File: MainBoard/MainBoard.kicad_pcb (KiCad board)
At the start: 2 copper layers, 39.6 x 110 mm, 29 parts, among them U1 TL074CN, U2 TL074CN, U3 TL074CN

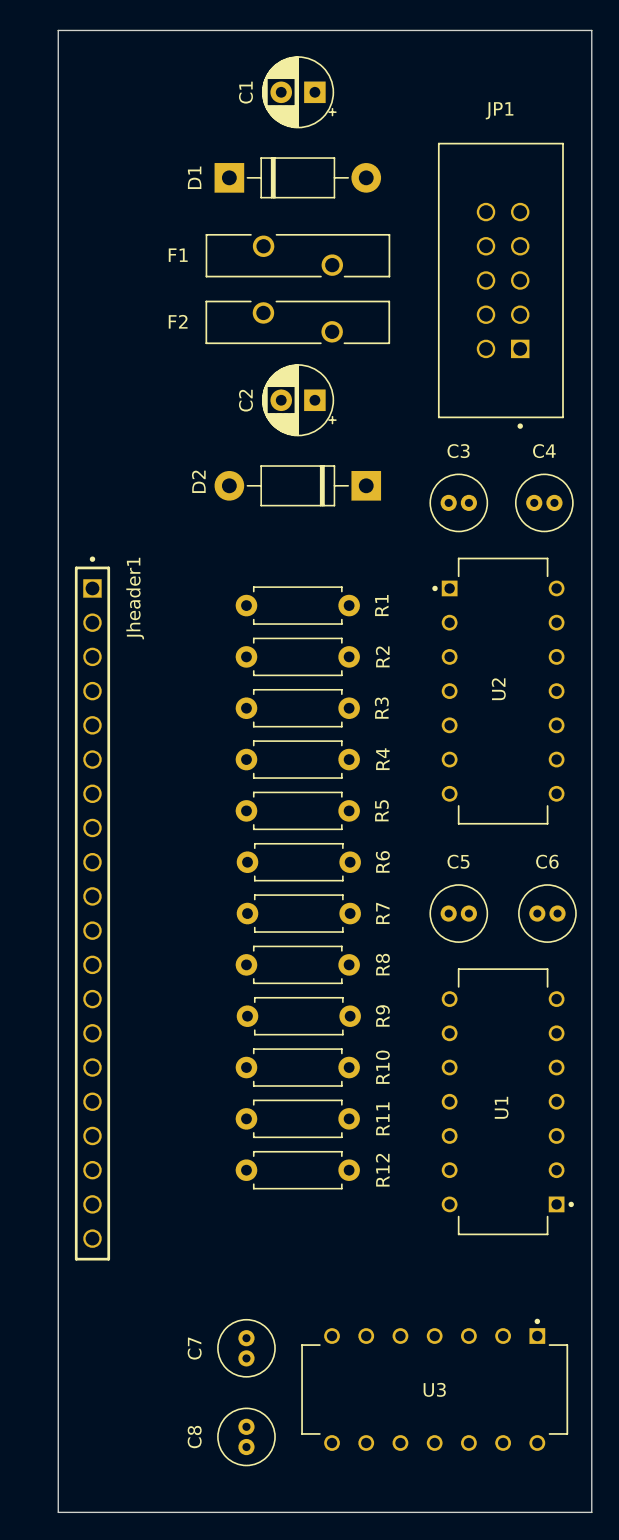
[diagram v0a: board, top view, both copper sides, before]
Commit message: updated with new footprints and 3d models
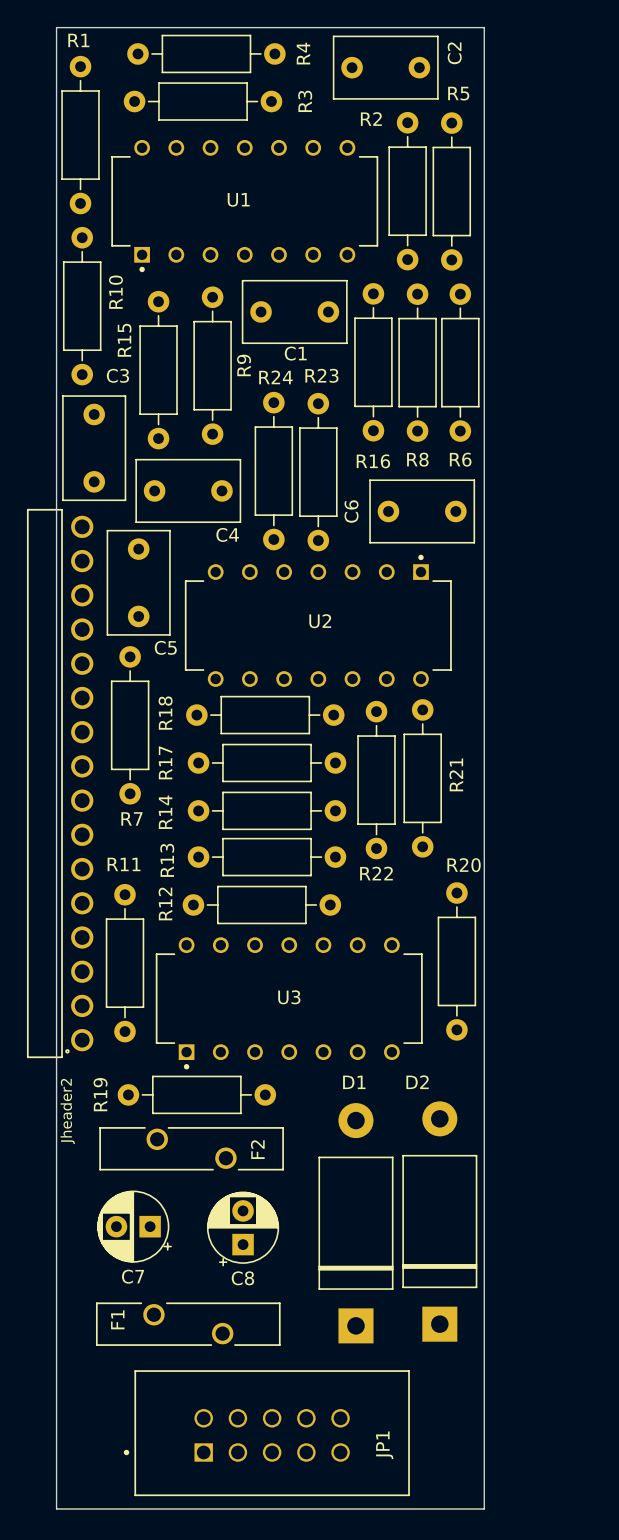
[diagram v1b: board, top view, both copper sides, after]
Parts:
- removed Jheader1: ESQ-120-12-T-S, ESQ-120-12-T-S:SAMTEC_ESQ-120-12-T-S
- added Jheader2: 61301611021, 61301611021:61301611021, F.Cu at (154.2, 98.3)
- added R13: 1k, Resistor_THT:R_Axial_DIN0207_L6.3mm_D2.5mm_P10.16mm_Horizontal, F.Cu at (162.8, 103.8)
- added R14: 1k, Resistor_THT:R_Axial_DIN0207_L6.3mm_D2.5mm_P10.16mm_Horizontal, F.Cu at (162.8, 100.3)
- added R15: 1M, Resistor_THT:R_Axial_DIN0207_L6.3mm_D2.5mm_P10.16mm_Horizontal, F.Cu at (159.8, 72.7)
- added R16: 100k, Resistor_THT:R_Axial_DIN0207_L6.3mm_D2.5mm_P10.16mm_Horizontal, F.Cu at (175.8, 62.0)
- added R17: 100k, Resistor_THT:R_Axial_DIN0207_L6.3mm_D2.5mm_P10.16mm_Horizontal, F.Cu at (173.0, 96.8)
- added R18: 100k, Resistor_THT:R_Axial_DIN0207_L6.3mm_D2.5mm_P10.16mm_Horizontal, F.Cu at (172.8, 93.2)
- added R19: 100k, Resistor_THT:R_Axial_DIN0207_L6.3mm_D2.5mm_P10.16mm_Horizontal, F.Cu at (167.8, 121.4)
- added R20: 100k, Resistor_THT:R_Axial_DIN0207_L6.3mm_D2.5mm_P10.16mm_Horizontal, F.Cu at (182.0, 116.6)
- added R21: 100k, Resistor_THT:R_Axial_DIN0207_L6.3mm_D2.5mm_P10.16mm_Horizontal, F.Cu at (179.5, 103.0)
- added R22: 100k, Resistor_THT:R_Axial_DIN0207_L6.3mm_D2.5mm_P10.16mm_Horizontal, F.Cu at (176.0, 93.0)
- added R23: 100k, Resistor_THT:R_Axial_DIN0207_L6.3mm_D2.5mm_P10.16mm_Horizontal, F.Cu at (171.7, 70.1)
- added R24: 100k, Resistor_THT:R_Axial_DIN0207_L6.3mm_D2.5mm_P10.16mm_Horizontal, F.Cu at (168.4, 70.0)
- C1, C2: value 10uf -> 0.1uf; footprint Capacitor_THT:CP_Radial_D5.0mm_P2.50mm -> Capacitor_THT:C_Disc_D7.5mm_W4.4mm_P5.00mm
- C3, C4, C5, C6: footprint Capacitor_THT:C_Radial_D4.0mm_H5.0mm_P1.50mm -> Capacitor_THT:C_Disc_D7.5mm_W4.4mm_P5.00mm
- C7, C8: value 0.1uf -> 10uf; footprint Capacitor_THT:C_Radial_D4.0mm_H5.0mm_P1.50mm -> Capacitor_THT:CP_Radial_D5.0mm_P2.50mm
- D1, D2: value 1N5818 -> 1N5934B; footprint Diode_THT:D_DO-41_SOD81_P10.16mm_Horizontal -> 1N5934B:P2_DO-201
- F1, F2: value Polyfuse -> type="R" model="Polyfuse" lib=""
- R1, R11, R12, R2, R3, R4, R5, R6, R7, R8: footprint Resistor_THT:R_Axial_DIN0207_L6.3mm_D2.5mm_P7.62mm_Horizontal -> Resistor_THT:R_Axial_DIN0207_L6.3mm_D2.5mm_P10.16mm_Horizontal
- R10, R9: value 1k -> 100k; footprint Resistor_THT:R_Axial_DIN0207_L6.3mm_D2.5mm_P7.62mm_Horizontal -> Resistor_THT:R_Axial_DIN0207_L6.3mm_D2.5mm_P10.16mm_Horizontal
- moved JP1 85.2 mm to (163.2, 148.0), turned to 0 degrees
- moved F1 79.7 mm to (162.1, 138.4)
- moved D1 78.2 mm to (174.5, 130.9), turned to 90 degrees
- moved U1 69.5 mm to (166.2, 55.1), turned to 90 degrees
- moved R10 62.8 mm to (154.2, 57.8), turned to -90 degrees
- moved F2 61.8 mm to (162.3, 125.4), turned to 180 degrees
- moved D2 54.9 mm to (180.7, 130.8), turned to 90 degrees
- moved R9 53.4 mm to (163.9, 62.2), turned to -90 degrees
- moved R5 53.3 mm to (181.6, 49.3), turned to -90 degrees
- moved R4 53.0 mm to (158.3, 44.1)
- moved R8 51.4 mm to (179.1, 62.0), turned to -90 degrees
- moved R3 45.8 mm to (158.1, 47.7)
- moved R6 45.0 mm to (182.2, 62.0), turned to -90 degrees
- moved R1 41.9 mm to (154.1, 45.1), turned to -90 degrees
- moved C5 36.5 mm to (158.4, 80.9), turned to -90 degrees
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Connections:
- C1 pad 2: -v -> GND
- C2 pad 2: Net-(C4-Pad1) -> GND
- C3 pad 2: -v -> GND
- C4 pad 1: Net-(C4-Pad1) -> -v
- C4 pad 2: -v -> GND
- C5 pad 2: -v -> GND
- C6 pad 1: Net-(C4-Pad1) -> -v
- C6 pad 2: -v -> GND
- C7 pad 2: -v -> GND
- C8 pad 1: Net-(C4-Pad1) -> GND
- D1 pad 2: -v -> GND
- D2 pad 1: -v -> GND
- D2 pad 2: Net-(C4-Pad1) -> -v
- F2 pad 1: Net-(C4-Pad1) -> -v
- JP1 pad 3: -v -> GND
- JP1 pad 4: -v -> GND
- JP1 pad 5: -v -> GND
- JP1 pad 6: -v -> GND
- JP1 pad 7: -v -> GND
- JP1 pad 8: -v -> GND
- R10 pad 1: Output6 -> Net-(U1-2IN+)
- R10 pad 2: Net-(R10-Pad2) -> InputBus1
- R11 pad 1: Output7 -> Output9
- R11 pad 2: Net-(R11-Pad2) -> Net-(U3-1IN-)
- R12 pad 1: Output8 -> Output12
- R5 pad 1: Output9 -> Output5
- R6 pad 1: Output10 -> Output6
- R7 pad 1: Output11 -> Output7
- R7 pad 2: Net-(R7-Pad2) -> Net-(U2-3IN-)
- R8 pad 1: Output12 -> Output8
- R8 pad 2: Net-(R7-Pad2) -> Net-(U2-4IN-)
- R9 pad 1: Output5 -> Net-(U1-1IN+)
- R9 pad 2: Net-(R9-Pad2) -> InputBus1
- U1 pad 10: InputBus1 -> Net-(U1-3IN+)
- U1 pad 3: InputBus1 -> Net-(U1-1IN+)
- U1 pad 5: InputBus1 -> Net-(U1-2IN+)
- U2 pad 10: InputBus4 -> Net-(U2-3IN+)
- U2 pad 12: InputBus4 -> Net-(U2-4IN+)
- U2 pad 13: Net-(R7-Pad2) -> Net-(U2-4IN-)
- U2 pad 14: Net-(R7-Pad2) -> Net-(U2-4IN-)
- U2 pad 3: InputBus3 -> Net-(U2-1IN+)
- U2 pad 5: InputBus4 -> Net-(U2-2IN+)
- U2 pad 8: Net-(U2-Pad8) -> Net-(U2-3IN-)
- U2 pad 9: Net-(U2-Pad8) -> Net-(U2-3IN-)
- U3 pad 1: Net-(R9-Pad2) -> Net-(U3-1IN-)
- U3 pad 10: InputBus3 -> Net-(U3-3IN+)
- U3 pad 12: InputBus3 -> Net-(U3-4IN+)
- U3 pad 2: Net-(R9-Pad2) -> Net-(U3-1IN-)
- U3 pad 3: InputBus2 -> Net-(U3-1IN+)
- U3 pad 5: InputBus2 -> Net-(U3-2IN+)
- U3 pad 6: Net-(R10-Pad2) -> Net-(U3-2IN-)
- U3 pad 7: Net-(R10-Pad2) -> Net-(U3-2IN-)
- U3 pad 8: Net-(R11-Pad2) -> Net-(U3-3IN-)
- U3 pad 9: Net-(R11-Pad2) -> Net-(U3-3IN-)
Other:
- board size 39.6 x 110 mm -> 31.8 x 110 mm

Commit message: updated placements
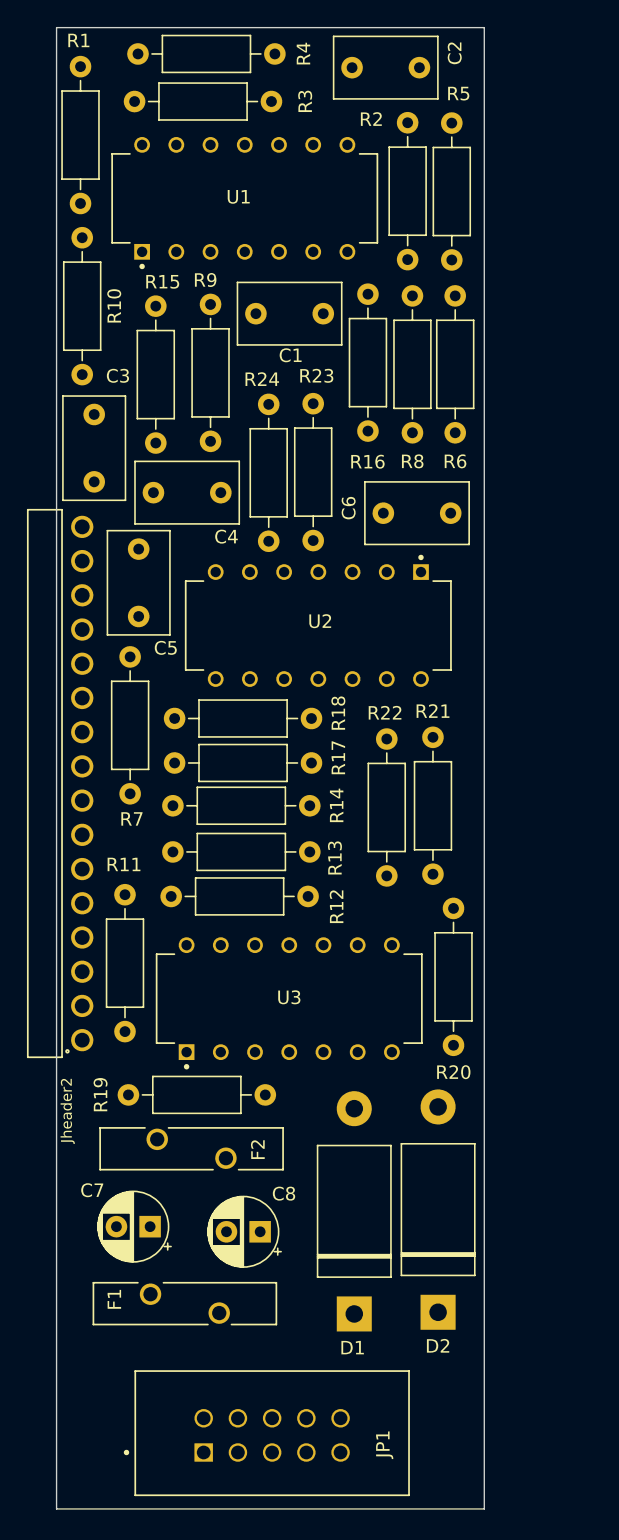
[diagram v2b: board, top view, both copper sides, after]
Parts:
- moved R21 2.17 mm to (180.2, 105.0)
- moved R22 2.17 mm to (176.8, 95.0)
- moved R13 1.94 mm to (160.9, 103.4)
- moved R14 1.94 mm to (160.9, 99.9)
- moved R17 1.78 mm to (171.2, 96.8)
- moved R12 1.77 mm to (170.9, 106.7)
- moved R18 1.67 mm to (171.2, 93.5)
- moved C8 1.59 mm to (167.4, 131.6), turned to 180 degrees
- moved F1 1.55 mm to (161.8, 136.9)
- moved R20 1.17 mm to (181.7, 117.7)
- moved D2 0.89 mm to (180.6, 129.9)
- moved D1 0.89 mm to (174.4, 130.0)
- moved R9 0.55 mm to (163.7, 62.7)
- moved R16 0.41 mm to (175.4, 62.0)
- moved C1 0.40 mm to (172.1, 63.4)
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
